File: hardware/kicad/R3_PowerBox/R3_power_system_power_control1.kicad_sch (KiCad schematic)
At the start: 7 parts, among them Q4 DMP3007LSS-13 SYSTEM LOAD SWI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, SW1 C&K RS282G05A3 / POWER ON

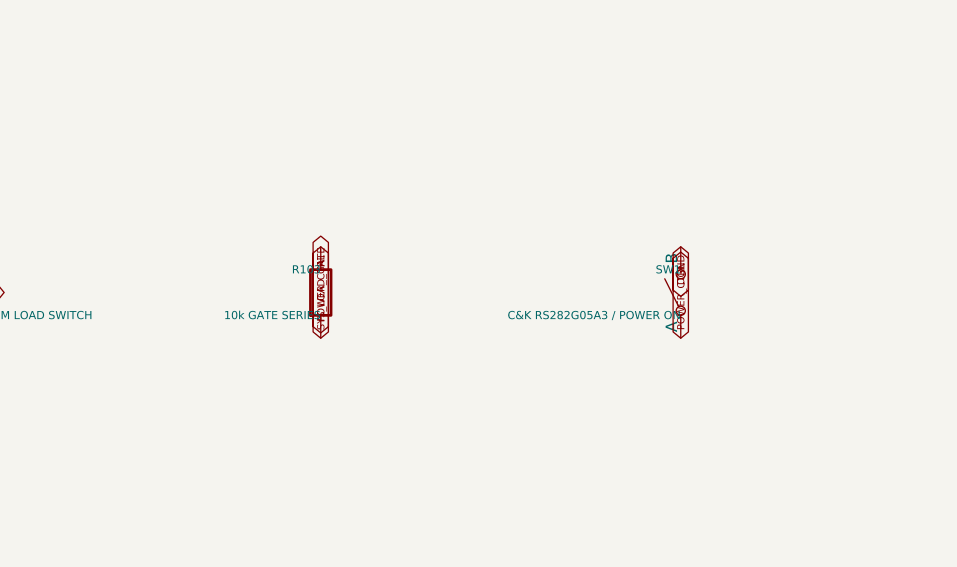
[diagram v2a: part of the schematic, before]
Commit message: Rev.A review fixes: initial schematic and component corrections
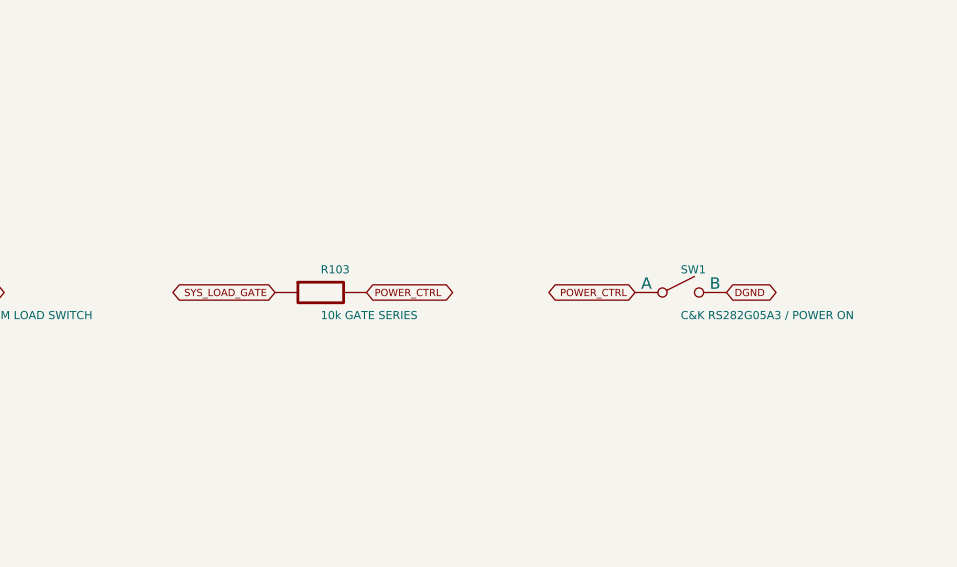
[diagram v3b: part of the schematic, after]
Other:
- moved on the sheet: R103, SW1
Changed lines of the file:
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@@
   (title_block
     (title "R3 PowerBox — power tree")
-    (date "2026-09-28")
+    (date "2026-10-03")
     (company "")
     (comment 1 "Generated with SKiDL")
@@
 	(global_label "SYS_LOAD_GATE"
 		(shape bidirectional)
-		(at 185 110.08 90)
-		(effects
-			(font
-				(size 0.8 0.8)
-			)
-			(justify left)
+		(at 179.92 105 180)
+		(effects
+			(font
+				(size 0.8 0.8)
+			)
+			(justify right)
 		)
 	)
 	(global_label "POWER_CTRL"
 		(shape bidirectional)
-		(at 185 99.92 270)
-		(effects
-			(font
-				(size 0.8 0.8)
-			)
-			(justify right)
+		(at 190.08 105 0)
+		(effects
+			(font
+				(size 0.8 0.8)
+			)
+			(justify left)
 		)
 	)
 	(global_label "POWER_CTRL"
 		(shape bidirectional)
-		(at 225 110.08 90)
-		(effects
-			(font
-				(size 0.8 0.8)
-			)
-			(justify left)
+		(at 219.92 105 180)
+		(effects
+			(font
+				(size 0.8 0.8)
+			)
+			(justify right)
 		)
 	)
 	(global_label "DGND"
 		(shape bidirectional)
-		(at 225 99.92 270)
-		(effects
-			(font
-				(size 0.8 0.8)
-			)
-			(justify right)
+		(at 230.08 105 0)
+		(effects
+			(font
+				(size 0.8 0.8)
+			)
+			(justify left)
 		)
 	)
@@
     (instances
       (project "SKiDL-Generated"
-        (path "/c950aac3-a7f8-40a1-8854-63ca2e6194cc/a9caf0ad-ee07-5321-84f1-7681c239e759"
+        (path "/7d40ec76-f97b-4a90-b5ea-ddf1628062b5/a9caf0ad-ee07-5321-84f1-7681c239e759"
           (reference "Q4")
           (unit 1)))))
@@
     (instances
       (project "SKiDL-Generated"
-        (path "/c950aac3-a7f8-40a1-8854-63ca2e6194cc/a9caf0ad-ee07-5321-84f1-7681c239e759"
+        (path "/7d40ec76-f97b-4a90-b5ea-ddf1628062b5/a9caf0ad-ee07-5321-84f1-7681c239e759"
           (reference "R102")
           (unit 1)))))
@@
     (instances
       (project "SKiDL-Generated"
-        (path "/c950aac3-a7f8-40a1-8854-63ca2e6194cc/a9caf0ad-ee07-5321-84f1-7681c239e759"
+        (path "/7d40ec76-f97b-4a90-b5ea-ddf1628062b5/a9caf0ad-ee07-5321-84f1-7681c239e759"
           (reference "C107")
           (unit 1)))))
   (symbol
     (lib_id "R3_POWER_GEN:R")
-    (at 185 105 90)
+    (at 185 105 0)
     (unit 1)
     (exclude_from_sim no)
@@
     (fields_autoplaced yes)
     (property "Reference" "R103"
-      (at 185 102.46 90)
+      (at 185 102.46 0)
       (effects
         (font
@@
         (justify left)))
     (property "Value" "10k GATE SERIES"
-      (at 185 107.54 90)
+      (at 185 107.54 0)
       (effects
         (font
@@
         (justify left)))
     (property "Footprint" "Resistor_SMD:R_0603_1608Metric"
-      (at 185 105 90)
-      (effects
-        (font
-          (size 0.9 0.9))
-        (hide yes)))
-    (property "Datasheet" "~"
-      (at 185 105 90)
-      (effects
-        (font
-          (size 0.9 0.9))
-        (hide yes)))
-    (property "Description" ""
-      (at 185 105 90)
-      (effects
-        (font
-          (size 0.9 0.9))
-        (hide yes)))
-    (pin "1"
-)
-    (pin "2"
-)
-    (instances
-      (project "SKiDL-Generated"
-        (path "/c950aac3-a7f8-40a1-8854-63ca2e6194cc/a9caf0ad-ee07-5321-84f1-7681c239e759"
+      (at 185 105 0)
+      (effects
+        (font
+          (size 0.9 0.9))
+        (hide yes)))
+    (property "Datasheet" "~"
+      (at 185 105 0)
+      (effects
+        (font
+          (size 0.9 0.9))
+        (hide yes)))
+    (property "Description" ""
+      (at 185 105 0)
+      (effects
+        (font
+          (size 0.9 0.9))
+        (hide yes)))
+    (pin "1"
+)
+    (pin "2"
+)
+    (instances
+      (project "SKiDL-Generated"
+        (path "/7d40ec76-f97b-4a90-b5ea-ddf1628062b5/a9caf0ad-ee07-5321-84f1-7681c239e759"
           (reference "R103")
           (unit 1)))))
   (symbol
     (lib_id "Switch:SW_SPST")
-    (at 225 105 90)
+    (at 225 105 0)
     (unit 1)
     (exclude_from_sim no)
@@
     (fields_autoplaced yes)
     (property "Reference" "SW1"
-      (at 225 102.46 90)
+      (at 225 102.46 0)
       (effects
         (font
@@
         (justify left)))
     (property "Value" "C&K RS282G05A3 / POWER ON"
-      (at 225 107.54 90)
+      (at 225 107.54 0)
       (effects
         (font
@@
         (justify left)))
     (property "Footprint" "Button_Switch_SMD:SW_SPST_CK_RS282G05A3"
-      (at 225 105 90)
-      (effects
-        (font
-          (size 0.9 0.9))
-        (hide yes)))
-    (property "Datasheet" "~"
-      (at 225 105 90)
+      (at 225 105 0)
+      (effects
+        (font
+          (size 0.9 0.9))
+        (hide yes)))
+    (property "Datasheet" "~"
+      (at 225 105 0)
       (effects
         (font
@@
         (hide yes)))
     (property "Description" "Single Pole Single Throw (SPST) switch"
-      (at 225 105 90)
-      (effects
-        (font
-          (size 0.9 0.9))
-        (hide yes)))
-    (pin "1"
-)
-    (pin "2"
-)
-    (instances
-      (project "SKiDL-Generated"
-        (path "/c950aac3-a7f8-40a1-8854-63ca2e6194cc/a9caf0ad-ee07-5321-84f1-7681c239e759"
+      (at 225 105 0)
+      (effects
+        (font
+          (size 0.9 0.9))
+        (hide yes)))
+    (pin "1"
+)
+    (pin "2"
+)
+    (instances
+      (project "SKiDL-Generated"
+        (path "/7d40ec76-f97b-4a90-b5ea-ddf1628062b5/a9caf0ad-ee07-5321-84f1-7681c239e759"
           (reference "SW1")
           (unit 1)))))
@@
     (instances
       (project "SKiDL-Generated"
-        (path "/c950aac3-a7f8-40a1-8854-63ca2e6194cc/a9caf0ad-ee07-5321-84f1-7681c239e759"
+        (path "/7d40ec76-f97b-4a90-b5ea-ddf1628062b5/a9caf0ad-ee07-5321-84f1-7681c239e759"
           (reference "C108")
           (unit 1)))))
@@
     (instances
       (project "SKiDL-Generated"
-        (path "/c950aac3-a7f8-40a1-8854-63ca2e6194cc/a9caf0ad-ee07-5321-84f1-7681c239e759"
+        (path "/7d40ec76-f97b-4a90-b5ea-ddf1628062b5/a9caf0ad-ee07-5321-84f1-7681c239e759"
           (reference "TP40")
           (unit 1)))))

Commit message: Rev.A review fixes: local charger power-stage reroute checkpoint
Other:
- moved on the sheet: R103, SW1
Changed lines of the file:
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@@
 	(global_label "SYS_LOAD_GATE"
 		(shape bidirectional)
-		(at 179.92 105 180)
+		(at 185 110.08 90)
+		(effects
+			(font
+				(size 0.8 0.8)
+			)
+			(justify left)
+		)
+	)
+	(global_label "POWER_CTRL"
+		(shape bidirectional)
+		(at 185 99.92 270)
 		(effects
 			(font
@@
 	(global_label "POWER_CTRL"
 		(shape bidirectional)
-		(at 190.08 105 0)
+		(at 225 110.08 90)
 		(effects
 			(font
@@
 		)
 	)
-	(global_label "POWER_CTRL"
-		(shape bidirectional)
-		(at 219.92 105 180)
+	(global_label "DGND"
+		(shape bidirectional)
+		(at 225 99.92 270)
 		(effects
 			(font
@@
 			)
 			(justify right)
-		)
-	)
-	(global_label "DGND"
-		(shape bidirectional)
-		(at 230.08 105 0)
-		(effects
-			(font
-				(size 0.8 0.8)
-			)
-			(justify left)
 		)
 	)
@@
     (instances
       (project "SKiDL-Generated"
-        (path "/7d40ec76-f97b-4a90-b5ea-ddf1628062b5/a9caf0ad-ee07-5321-84f1-7681c239e759"
+        (path "/2b0a7443-ac4c-4207-8273-267cee2a0847/a9caf0ad-ee07-5321-84f1-7681c239e759"
           (reference "Q4")
           (unit 1)))))
@@
     (instances
       (project "SKiDL-Generated"
-        (path "/7d40ec76-f97b-4a90-b5ea-ddf1628062b5/a9caf0ad-ee07-5321-84f1-7681c239e759"
+        (path "/2b0a7443-ac4c-4207-8273-267cee2a0847/a9caf0ad-ee07-5321-84f1-7681c239e759"
           (reference "R102")
           (unit 1)))))
@@
     (instances
       (project "SKiDL-Generated"
-        (path "/7d40ec76-f97b-4a90-b5ea-ddf1628062b5/a9caf0ad-ee07-5321-84f1-7681c239e759"
+        (path "/2b0a7443-ac4c-4207-8273-267cee2a0847/a9caf0ad-ee07-5321-84f1-7681c239e759"
           (reference "C107")
           (unit 1)))))
   (symbol
     (lib_id "R3_POWER_GEN:R")
-    (at 185 105 0)
+    (at 185 105 90)
     (unit 1)
     (exclude_from_sim no)
@@
     (fields_autoplaced yes)
     (property "Reference" "R103"
-      (at 185 102.46 0)
+      (at 185 102.46 90)
       (effects
         (font
@@
         (justify left)))
     (property "Value" "10k GATE SERIES"
-      (at 185 107.54 0)
+      (at 185 107.54 90)
       (effects
         (font
@@
         (justify left)))
     (property "Footprint" "Resistor_SMD:R_0603_1608Metric"
-      (at 185 105 0)
-      (effects
-        (font
-          (size 0.9 0.9))
-        (hide yes)))
-    (property "Datasheet" "~"
-      (at 185 105 0)
-      (effects
-        (font
-          (size 0.9 0.9))
-        (hide yes)))
-    (property "Description" ""
-      (at 185 105 0)
-      (effects
-        (font
-          (size 0.9 0.9))
-        (hide yes)))
-    (pin "1"
-)
-    (pin "2"
-)
-    (instances
-      (project "SKiDL-Generated"
-        (path "/7d40ec76-f97b-4a90-b5ea-ddf1628062b5/a9caf0ad-ee07-5321-84f1-7681c239e759"
+      (at 185 105 90)
+      (effects
+        (font
+          (size 0.9 0.9))
+        (hide yes)))
+    (property "Datasheet" "~"
+      (at 185 105 90)
+      (effects
+        (font
+          (size 0.9 0.9))
+        (hide yes)))
+    (property "Description" ""
+      (at 185 105 90)
+      (effects
+        (font
+          (size 0.9 0.9))
+        (hide yes)))
+    (pin "1"
+)
+    (pin "2"
+)
+    (instances
+      (project "SKiDL-Generated"
+        (path "/2b0a7443-ac4c-4207-8273-267cee2a0847/a9caf0ad-ee07-5321-84f1-7681c239e759"
           (reference "R103")
           (unit 1)))))
   (symbol
     (lib_id "Switch:SW_SPST")
-    (at 225 105 0)
+    (at 225 105 90)
     (unit 1)
     (exclude_from_sim no)
@@
     (fields_autoplaced yes)
     (property "Reference" "SW1"
-      (at 225 102.46 0)
+      (at 225 102.46 90)
       (effects
         (font
@@
         (justify left)))
     (property "Value" "C&K RS282G05A3 / POWER ON"
-      (at 225 107.54 0)
+      (at 225 107.54 90)
       (effects
         (font
@@
         (justify left)))
     (property "Footprint" "Button_Switch_SMD:SW_SPST_CK_RS282G05A3"
-      (at 225 105 0)
-      (effects
-        (font
-          (size 0.9 0.9))
-        (hide yes)))
-    (property "Datasheet" "~"
-      (at 225 105 0)
+      (at 225 105 90)
+      (effects
+        (font
+          (size 0.9 0.9))
+        (hide yes)))
+    (property "Datasheet" "~"
+      (at 225 105 90)
       (effects
         (font
@@
         (hide yes)))
     (property "Description" "Single Pole Single Throw (SPST) switch"
-      (at 225 105 0)
-      (effects
-        (font
-          (size 0.9 0.9))
-        (hide yes)))
-    (pin "1"
-)
-    (pin "2"
-)
-    (instances
-      (project "SKiDL-Generated"
-        (path "/7d40ec76-f97b-4a90-b5ea-ddf1628062b5/a9caf0ad-ee07-5321-84f1-7681c239e759"
+      (at 225 105 90)
+      (effects
+        (font
+          (size 0.9 0.9))
+        (hide yes)))
+    (pin "1"
+)
+    (pin "2"
+)
+    (instances
+      (project "SKiDL-Generated"
+        (path "/2b0a7443-ac4c-4207-8273-267cee2a0847/a9caf0ad-ee07-5321-84f1-7681c239e759"
           (reference "SW1")
           (unit 1)))))
@@
     (instances
       (project "SKiDL-Generated"
-        (path "/7d40ec76-f97b-4a90-b5ea-ddf1628062b5/a9caf0ad-ee07-5321-84f1-7681c239e759"
+        (path "/2b0a7443-ac4c-4207-8273-267cee2a0847/a9caf0ad-ee07-5321-84f1-7681c239e759"
           (reference "C108")
           (unit 1)))))
@@
     (instances
       (project "SKiDL-Generated"
-        (path "/7d40ec76-f97b-4a90-b5ea-ddf1628062b5/a9caf0ad-ee07-5321-84f1-7681c239e759"
+        (path "/2b0a7443-ac4c-4207-8273-267cee2a0847/a9caf0ad-ee07-5321-84f1-7681c239e759"
           (reference "TP40")
           (unit 1)))))
